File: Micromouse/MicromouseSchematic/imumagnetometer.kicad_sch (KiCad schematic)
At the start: 6 parts, among them U3 ICM-42688-P, U4 LIS2MDLTR

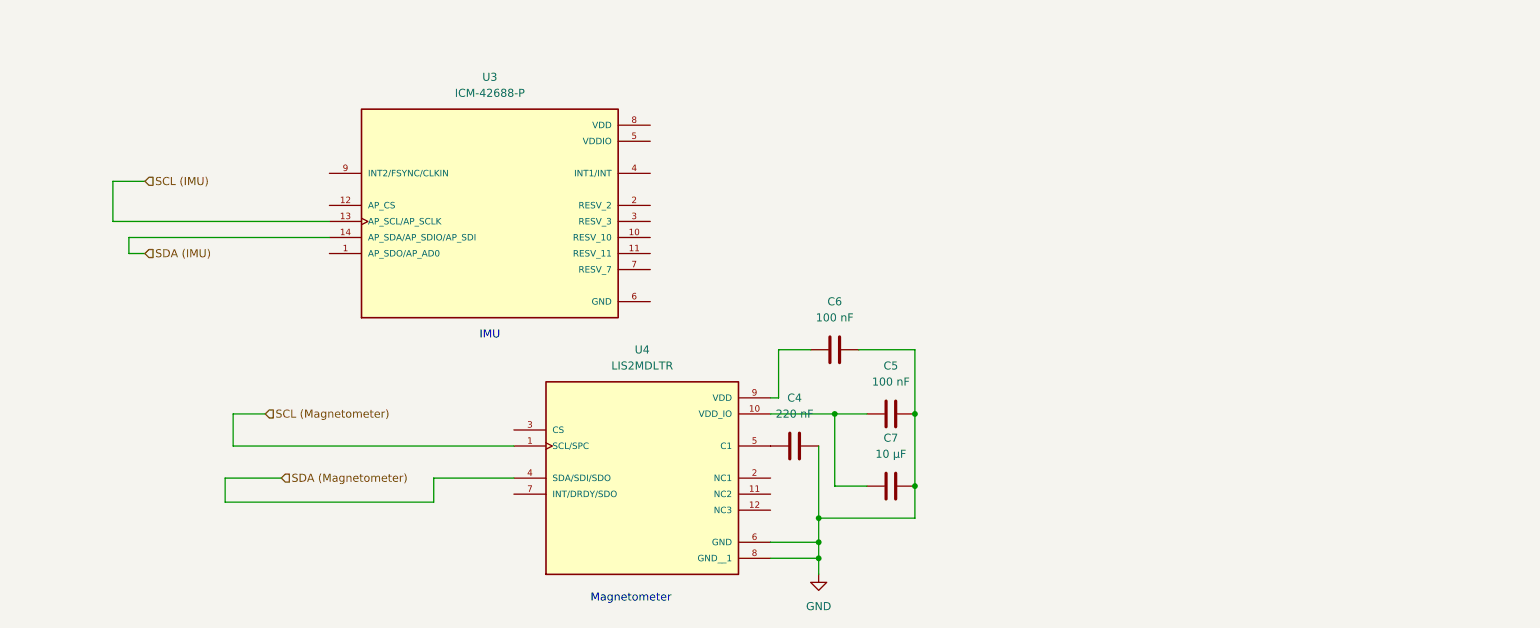
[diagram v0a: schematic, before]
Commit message: Updated IMU and Magnetometer schematics
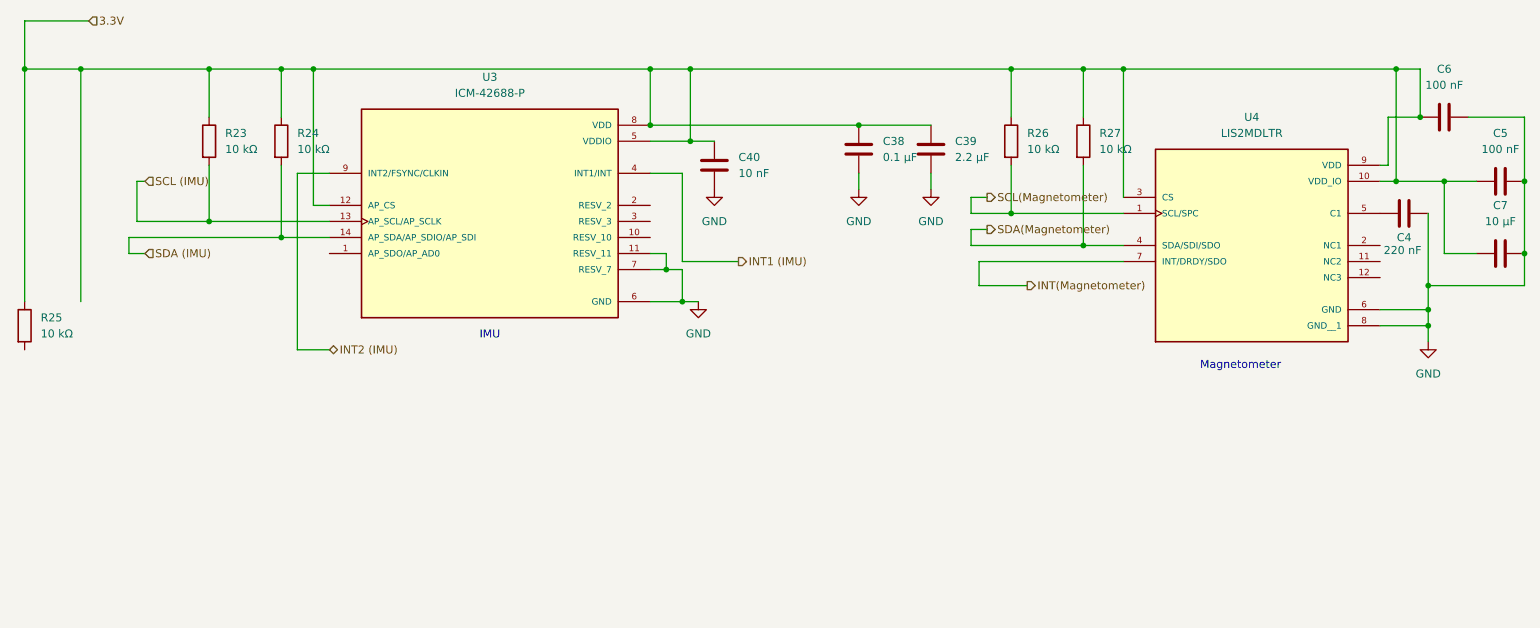
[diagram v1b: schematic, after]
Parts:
- added C38: 0.1 μF, symbol Device:C
- added C39: 2.2 μF, symbol Device:C
- added C40: 10 nF, symbol Device:C
- added R23, R24, R25, R26, R27: 10 kΩ, symbol Device:R
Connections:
- net GND: now also U3.11 (RESV_11), U3.6 (GND), U3.7 (RESV_7), C38.2, C39.2, C40.2
- net SCL (IMU): now also R23.2
- net SDA (IMU): now also R24.2
- net 3.3V: now reaches C6.1, U4.9 (VDD)
- net 3.3V: now also C5.1, C7.1, U3.12 (AP_CS), U3.5 (VDDIO), U3.8 (VDD), U4.10 (VDD_IO), U4.3 (CS), C38.1, C39.1, C40.1, R23.1, R24.1, R25.1, R26.1, R27.1
- net INT(Magnetometer): now reaches U4.7 (INT/DRDY/SDO)
- net INT1 (IMU): now reaches U3.4 (INT1/INT)
- net INT2 (IMU): now reaches U3.9 (INT2/FSYNC/CLKIN)
- net SCL (Magnetometer) renamed SCL(Magnetometer)
- net SCL(Magnetometer): now also R26.2
- net SDA (Magnetometer) renamed SDA(Magnetometer)
- net SDA(Magnetometer): now also R27.2
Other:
- moved on the sheet: C4, C5, C6, C7, U4

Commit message: Made changesto IMU/magnetometer
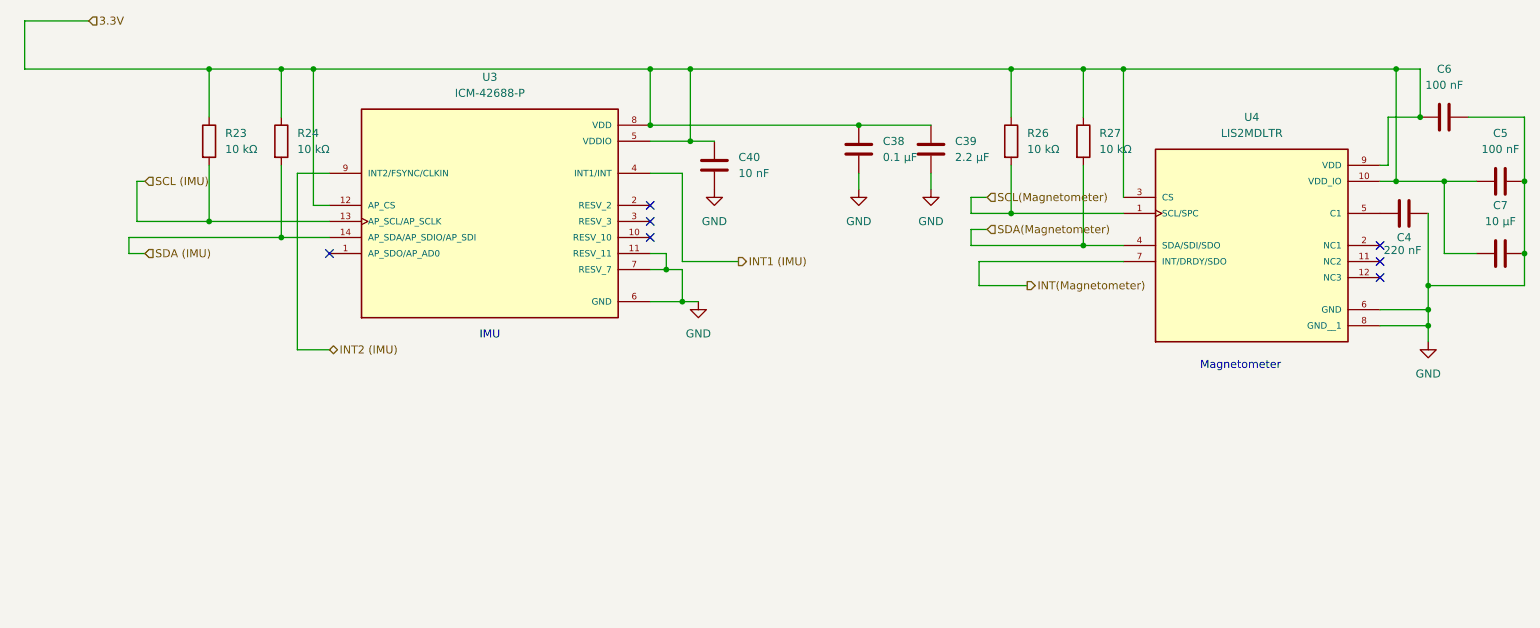
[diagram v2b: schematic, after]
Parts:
- removed R25: 10 kΩ, symbol Device:R
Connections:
- no-connect marks 0 -> 7
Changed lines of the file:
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@@
-	)
-	(junction
-		(at 43.18 58.42)
-		(diameter 0)
-		(color 0 0 0 0)
 	)
 	(junction
@@
 	)
 	(junction
-		(at 34.29 58.42)
-		(diameter 0)
-		(color 0 0 0 0)
-	)
-	(junction
 		(at 139.7 58.42)
 		(diameter 0)
 		(color 0 0 0 0)
 	)
+	(no_connect
+		(at 82.55 87.63)
+	)
+	(no_connect
+		(at 248.92 88.9)
+	)
+	(no_connect
+		(at 248.92 86.36)
+	)
+	(no_connect
+		(at 133.35 80.01)
+	)
+	(no_connect
+		(at 133.35 85.09)
+	)
+	(no_connect
+		(at 133.35 82.55)
+	)
+	(no_connect
+		(at 248.92 91.44)
+	)
 	(wire
 		(pts
@@
 	(wire
 		(pts
-			(xy 34.29 58.42) (xy 43.18 58.42)
+			(xy 34.29 58.42) (xy 63.5 58.42)
 		)
 		(stroke
@@
 	(wire
 		(pts
-			(xy 43.18 58.42) (xy 63.5 58.42)
-		)
-		(stroke
-			(width 0)
-			(type default)
-		)
-	)
-	(wire
-		(pts
 			(xy 133.35 69.85) (xy 139.7 69.85)
 		)
@@
 	(wire
 		(pts
-			(xy 34.29 95.25) (xy 34.29 58.42)
-		)
-		(stroke
-			(width 0)
-			(type default)
-		)
-	)
-	(wire
-		(pts
 			(xy 80.01 58.42) (xy 133.35 58.42)
 		)
@@
 		(pts
 			(xy 208.28 81.28) (xy 190.5 81.28)
-		)
-		(stroke
-			(width 0)
-			(type default)
-		)
-	)
-	(wire
-		(pts
-			(xy 43.18 58.42) (xy 43.18 95.25)
 		)
 		(stroke
@@
 	)
 	(hierarchical_label "SDA(Magnetometer)"
-		(shape output)
+		(shape input)
 		(at 186.69 83.82 0)
 		(effects
@@
 	)
 	(hierarchical_label "SCL(Magnetometer)"
-		(shape output)
+		(shape input)
 		(at 186.69 78.74 0)
 		(effects
@@
 					(unit 1)
 				)
-			)
-		)
-	)
-	(symbol
-		(lib_id "Device:R")
-		(at 34.29 99.06 0)
-		(unit 1)
-		(exclude_from_sim no)
-		(in_bom yes)
-		(on_board yes)
-		(dnp no)
-		(fields_autoplaced yes)
-		(property "Reference" "R25"
-			(at 36.83 97.7899 0)
-			(effects
-				(font
-					(size 1.27 1.27)
-				)
-				(justify left)
-			)
-		)
-		(property "Value" "10 kΩ"
-			(at 36.83 100.3299 0)
-			(effects
-				(font
-					(size 1.27 1.27)
-				)
-				(justify left)
-			)
-		)
-		(property "Footprint" ""
-			(at 32.512 99.06 90)
-			(effects
-				(font
-					(size 1.27 1.27)
-				)
-				(hide yes)
-			)
-		)
-		(property "Datasheet" "~"
-			(at 34.29 99.06 0)
-			(effects
-				(font
-					(size 1.27 1.27)
-				)
-				(hide yes)
-			)
-		)
-		(property "Description" "Resistor"
-			(at 34.29 99.06 0)
-			(effects
-				(font
-					(size 1.27 1.27)
-				)
-				(hide yes)
-			)
-		)
-		(pin "1"
-		)
-		(pin "2"
-		)
-		(instances
-			(project "MicromouseSchematic"
-				(path "/0dcfab91-6b00-43c0-ac0b-8c301cb559e5/020b5f85-8a9d-45f7-80e4-737602419b71"
-					(reference "R25")
-					(unit 1)
-				)

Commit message: added some stuff
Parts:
- U3: footprint ICM-42688-P:PQFN50P300X250X97-14N -> ICM_42688_P_FOOTPRINT:ICM_42688_P; symbol ICM42688:ICM-42688-P -> ICM-42688-P:ICM-42688-P
- U4: symbol LIS2MDL:LIS2MDLTR -> LIS2MDLTR:LIS2MDLTR

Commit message: updated stuff
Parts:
- U4: footprint LIS2MDLTR:PQFN50P200X200X70-12N -> LIS2MDLTR_FOOTPRINT:LIS2MDLTR
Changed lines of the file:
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@@
 			)
 		)
-		(property "Footprint" "LIS2MDLTR:PQFN50P200X200X70-12N"
+		(property "Footprint" "LIS2MDLTR_FOOTPRINT:LIS2MDLTR"
 			(at 228.6 83.82 0)
 			(effects

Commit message: Micromouse KiCad: MP6550 libs in project, fp-lib paths, schematic updates
Move MP6550G-Z symbol and legacy footprints into MicromouseSchematic, add
MP6550G-Z.pretty with MP6550_MNP footprint, and point fp-lib-table at the
project-local MM_MP6550G-Z library.

Replace old absolute footprint paths with this repo’s Micromouse tree and
MM_* library names. Update root schematic and IMU/IR/motor/TOF/regulator
subsheets; add empty bluethooth.kicad_sch hierarchical sheet. Extend KiCad
project BOM field configuration; refresh fp-info-cache. Drop schematic lock
file; include dated schematic backup zip.
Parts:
- U3: footprint ICM_42688_P_FOOTPRINT:ICM_42688_P -> MM_ICM_42688_P:ICM_42688_P
- U4: footprint LIS2MDLTR_FOOTPRINT:LIS2MDLTR -> MM_LIS2MDLTR:LIS2MDLTR
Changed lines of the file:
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@@
 			)
 		)
-		(property "Footprint" "LIS2MDLTR_FOOTPRINT:LIS2MDLTR"
+		(property "Footprint" "MM_LIS2MDLTR:LIS2MDLTR"
 			(at 228.6 83.82 0)
 			(effects
@@
 			)
 		)
-		(property "Footprint" "ICM_42688_P_FOOTPRINT:ICM_42688_P"
+		(property "Footprint" "MM_ICM_42688_P:ICM_42688_P"
 			(at 107.95 80.01 0)
 			(effects

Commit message: Micromouse KiCad: STM32-centric routing; ERC errors 23→6; backups and gitignore
Body:
Connected almost all STM32 signals; ERC down to 6

Rework root schematic plus motor driver, IMU/magnetometer, IR sensor, and TOF
subsheets so the bulk of signals reach the STM32. KiCad ERC is not fully clean
yet, but major nets are in place: errors dropped from 23 to 6 while many
previously unconnected signals were wired.

Add 2026-04-08 schematic backup zips. Extend .gitignore for macOS .DS_Store
paths. Update MicromouseSchematic.kicad_prl.
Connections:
- net SCL(Magnetometer) is gone; now on net SCL (IMU): R26.2, U4.1 (SCL/SPC)
- net SDA(Magnetometer) is gone; now on net SDA (IMU): R27.2, U4.4 (SDA/SDI/SDO)
- net GND: now also U3.1 (AP_SDO/AP_AD0)
- no-connect marks 7 -> 6
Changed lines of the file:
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@@
+	)
+	(junction
+		(at 88.9 120.65)
+		(diameter 0)
+		(color 0 0 0 0)
 	)
 	(junction
@@
 	)
 	(junction
+		(at 133.35 121.92)
+		(diameter 0)
+		(color 0 0 0 0)
+	)
+	(junction
 		(at 271.78 87.63)
 		(diameter 0)
@@
 		(diameter 0)
 		(color 0 0 0 0)
-	)
-	(no_connect
-		(at 82.55 87.63)
 	)
 	(no_connect
@@
 	(wire
 		(pts
+			(xy 80.01 88.9) (xy 80.01 87.63)
+		)
+		(stroke
+			(width 0)
+			(type default)
+		)
+	)
+	(wire
+		(pts
 			(xy 256.54 99.06) (xy 256.54 101.6)
 		)
@@
 	(wire
 		(pts
+			(xy 88.9 120.65) (xy 88.9 125.73)
+		)
+		(stroke
+			(width 0)
+			(type default)
+		)
+	)
+	(wire
+		(pts
 			(xy 256.54 81.28) (xy 256.54 92.71)
 		)
@@
 	(wire
 		(pts
+			(xy 133.35 121.92) (xy 129.54 121.92)
+		)
+		(stroke
+			(width 0)
+			(type default)
+		)
+	)
+	(wire
+		(pts
 			(xy 201.93 86.36) (xy 208.28 86.36)
 		)
@@
 	(wire
 		(pts
+			(xy 92.71 120.65) (xy 88.9 120.65)
+		)
+		(stroke
+			(width 0)
+			(type default)
+		)
+	)
+	(wire
+		(pts
 			(xy 74.93 58.42) (xy 74.93 66.04)
 		)
@@
 	(wire
 		(pts
+			(xy 80.01 87.63) (xy 82.55 87.63)
+		)
+		(stroke
+			(width 0)
+			(type default)
+		)
+	)
+	(wire
+		(pts
 			(xy 138.43 74.93) (xy 138.43 88.9)
 		)
@@
 	(wire
 		(pts
+			(xy 88.9 120.65) (xy 85.09 120.65)
+		)
+		(stroke
+			(width 0)
+			(type default)
+		)
+	)
+	(wire
+		(pts
 			(xy 190.5 58.42) (xy 201.93 58.42)
 		)
@@
 		(pts
 			(xy 77.47 102.87) (xy 82.55 102.87)
+		)
+		(stroke
+			(width 0)
+			(type default)
+		)
+	)
+	(wire
+		(pts
+			(xy 137.16 121.92) (xy 133.35 121.92)
+		)
+		(stroke
+			(width 0)
+			(type default)
+		)
+	)
+	(wire
+		(pts
+			(xy 133.35 121.92) (xy 133.35 127)
 		)
 		(stroke
@@
 		)
 	)
+	(hierarchical_label "SCL (IMU)"
+		(shape input)
+		(at 85.09 120.65 180)
+		(effects
+			(font
+				(size 1.27 1.27)
+			)
+			(justify right)
+		)
+	)
+	(hierarchical_label "SDA(Common)"
+		(shape input)
+		(at 133.35 127 0)
+		(effects
+			(font
+				(size 1.27 1.27)
+			)
+			(justify left)
+		)
+	)
 	(hierarchical_label "SDA (IMU)"
 		(shape input)
@@
 		)
 	)
+	(hierarchical_label "SCL(Magnetometer)"
+		(shape input)
+		(at 92.71 120.65 0)
+		(effects
+			(font
+				(size 1.27 1.27)
+			)
+			(justify left)
+		)
+	)
+	(hierarchical_label "SCL(Common)"
+		(shape input)
+		(at 88.9 125.73 0)
+		(effects
+			(font
+				(size 1.27 1.27)
+			)
+			(justify left)
+		)
+	)
 	(hierarchical_label "INT(Magnetometer)"
 		(shape output)
@@
 			)
 			(justify left)
+		)
+	)
+	(hierarchical_label "SDA(Magnetometer)"
+		(shape input)
+		(at 137.16 121.92 0)
+		(effects
+			(font
+				(size 1.27 1.27)
+			)
+			(justify left)
+		)
+	)
+	(hierarchical_label "SDA (IMU)"
+		(shape input)
+		(at 129.54 121.92 180)
+		(effects
+			(font
+				(size 1.27 1.27)
+			)
+			(justify right)
 		)
 	)
@@
 					(unit 1)
 				)
+			)
+		)
+	)
+	(symbol
+		(lib_id "power:GND")
+		(at 80.01 88.9 0)
+		(unit 1)
+		(exclude_from_sim no)
+		(in_bom yes)
+		(on_board yes)
+		(dnp no)
+		(fields_autoplaced yes)
+		(property "Reference" "#PWR012"
+			(at 80.01 95.25 0)
+			(effects
+				(font
+					(size 1.27 1.27)
+				)
+				(hide yes)
+			)
+		)
+		(property "Value" "GND"
+			(at 80.01 93.98 0)
+			(effects
+				(font
+					(size 1.27 1.27)
+				)
+			)
+		)
+		(property "Footprint" ""
+			(at 80.01 88.9 0)
+			(effects
+				(font
+					(size 1.27 1.27)
+				)
+				(hide yes)
+			)
+		)
+		(property "Datasheet" ""
+			(at 80.01 88.9 0)
+			(effects
+				(font
+					(size 1.27 1.27)
+				)
+				(hide yes)
+			)
+		)
+		(property "Description" "Power symbol creates a global label with name \"GND\" , ground"
+			(at 80.01 88.9 0)
+			(effects
+				(font
+					(size 1.27 1.27)
+				)
+				(hide yes)
+			)
+		)
+		(pin "1"
+		)
+		(instances
+			(project "MicromouseSchematic"
+				(path "/0dcfab91-6b00-43c0-ac0b-8c301cb559e5/020b5f85-8a9d-45f7-80e4-737602419b71"
+					(reference "#PWR012")
+					(unit 1)
+				)

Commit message: Micromouse KiCad: MP6550 layout, schematic updates; ERC clean, warnings ~5–6
Relocate MP6550G-Z symbol and footprint trees from MicromouseSchematic into
Micromouse/MP6550G-Z and refresh sym-lib-table (portable ${KIPRJMOD} paths
where applicable, MP6550 at new location).

Update root schematic plus IMU, IR, motor driver, and TOF subsheets. KiCad
ERC: all errors resolved (previously 6 remaining after earlier bring-up).
Warnings reduced from roughly 35–40+ down to about 5–6.

Add MicromouseSchematic-2026-04-11_212024.zip backup.
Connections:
- net SCL (IMU) renamed SCL (Common)
- net SDA (IMU) renamed SDA(Common)
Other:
- moved on the sheet: C38, C39
